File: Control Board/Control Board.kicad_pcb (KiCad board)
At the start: 2 copper layers, 80 x 58.4 mm, 97 parts, among them J1 Conn_02x10_Odd_Even, J10 Conn_01x03, J11 Conn_01x03, J13 Conn_01x03, J14 Conn_01x03, J15 Conn_01x03, J2 Conn_02x03_Odd_Even, J3 RJ45, J4 Conn_01x02, J5 Conn_01x02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

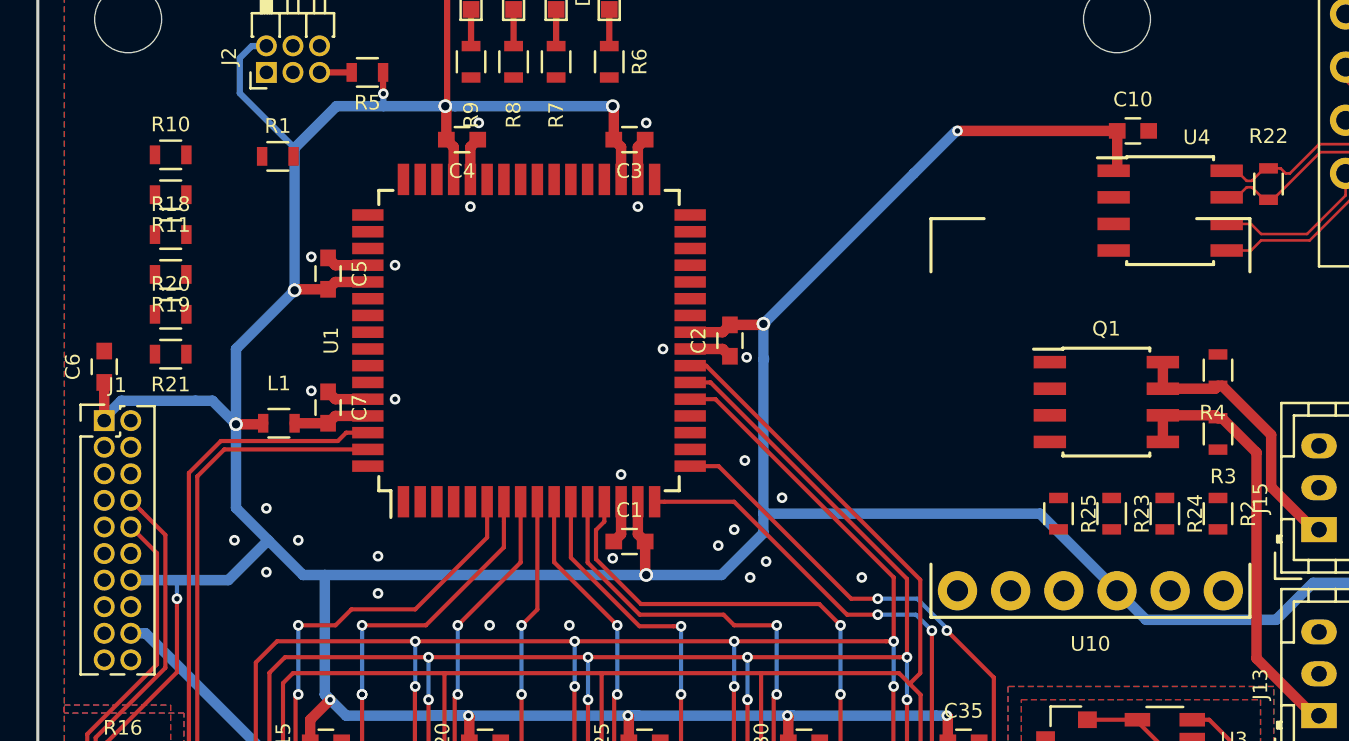
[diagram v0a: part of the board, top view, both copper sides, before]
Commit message: Added comments and stuff for power board PCB review
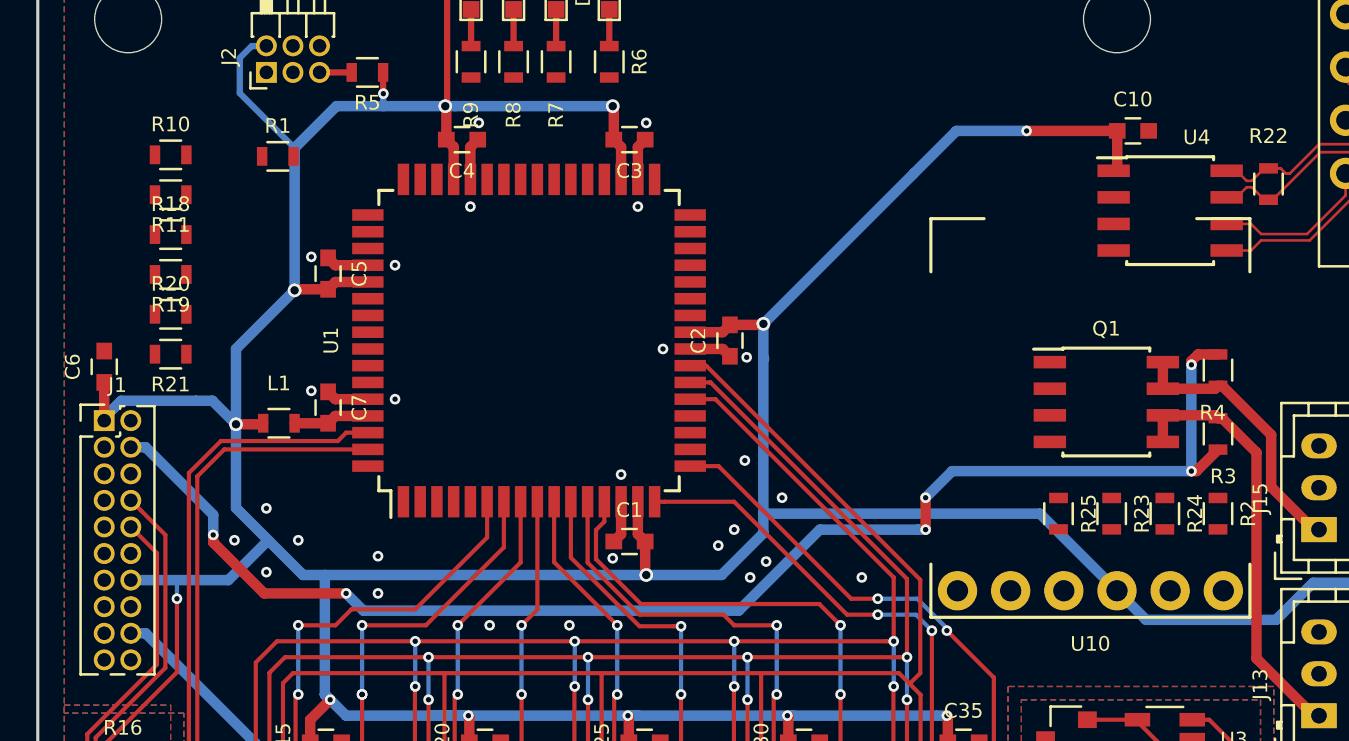
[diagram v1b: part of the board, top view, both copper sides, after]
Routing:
- net /VCC_IN: track 0.00 -> 66.7 mm, vias 0 -> 6
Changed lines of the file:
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@@
     (thickness 1.6)
     (drawings 25)
-    (tracks 765)
+    (tracks 794)
     (zones 0)
     (modules 97)
@@
     (effects (font (size 1 1) (thickness 0.15)) (justify left mirror))
   )
+  (segment (start 223.773996 109.982) (end 220.418 109.982) (width 0.5) (layer B.Cu) (net 1))
+  (segment (start 228.104 109.982) (end 223.773996 109.982) (width 0.5) (layer F.Cu) (net 1))
+  (via (at 223.773996 109.982) (size 0.508) (drill 0.254) (layers F.Cu B.Cu) (net 1))
   (segment (start 245.11 137.922) (end 244.86 137.922) (width 0.5) (layer B.Cu) (net 1))
   (segment (start 244.86 137.922) (end 242.32 135.382) (width 0.5) (layer B.Cu) (net 1))
@@
   (segment (start 244.86 129.032) (end 245.11 129.032) (width 0.5) (layer B.Cu) (net 1))
   (segment (start 218.386 112.014) (end 220.418 109.982) (width 0.5) (layer B.Cu) (net 1))
-  (segment (start 228.104 109.982) (end 220.472 109.982) (width 0.5) (layer F.Cu) (net 1))
-  (via (at 220.472 109.982) (size 0.508) (drill 0.254) (layers F.Cu B.Cu) (net 1))
   (segment (start 228.104 109.982) (end 228.104 111.715) (width 0.5) (layer F.Cu) (net 1))
   (segment (start 228.104 111.715) (end 227.932 111.887) (width 0.5) (layer F.Cu) (net 1))
@@
   (via (at 188.976 133.604) (size 0.508) (drill 0.254) (layers F.Cu B.Cu) (net 68))
   (segment (start 188.976 136.906) (end 188.976 133.604) (width 0.2) (layer B.Cu) (net 68))
+  (segment (start 231.648 120.982) (end 231.648 121.158006) (width 0.5) (layer F.Cu) (net 69))
+  (segment (start 232.918 120.662) (end 231.968 120.662) (width 0.5) (layer F.Cu) (net 69))
+  (segment (start 231.968 120.662) (end 231.648 120.982) (width 0.5) (layer F.Cu) (net 69))
+  (segment (start 231.648 126.238) (end 231.648 121.158006) (width 0.5) (layer B.Cu) (net 69))
+  (via (at 231.648 121.158006) (size 0.508) (drill 0.254) (layers F.Cu B.Cu) (net 69))
+  (segment (start 231.648 126.238) (end 231.89 126.238) (width 0.5) (layer F.Cu) (net 69))
+  (segment (start 231.89 126.238) (end 232.918 125.21) (width 0.5) (layer F.Cu) (net 69))
+  (segment (start 218.948 127.508) (end 220.218 126.238) (width 0.5) (layer B.Cu) (net 69))
+  (segment (start 220.218 126.238) (end 231.648 126.238) (width 0.5) (layer B.Cu) (net 69))
+  (via (at 231.648 126.238) (size 0.508) (drill 0.254) (layers F.Cu B.Cu) (net 69))
+  (segment (start 218.948006 129.032) (end 218.948006 127.508006) (width 0.5) (layer F.Cu) (net 69))
+  (via (at 218.948 127.508) (size 0.508) (drill 0.254) (layers F.Cu B.Cu) (net 69))
+  (segment (start 218.948006 127.508006) (end 218.948 127.508) (width 0.5) (layer F.Cu) (net 69))
+  (via (at 184.912 129.286) (size 0.508) (drill 0.254) (layers F.Cu B.Cu) (net 69))
+  (segment (start 184.912 128.324894) (end 184.912 129.286) (width 0.5) (layer B.Cu) (net 69))
+  (segment (start 181.682106 125.095) (end 184.912 128.324894) (width 0.5) (layer B.Cu) (net 69))
+  (segment (start 180.975 125.095) (end 181.682106 125.095) (width 0.5) (layer B.Cu) (net 69))
+  (via (at 191.262 132.08) (size 0.508) (drill 0.254) (layers F.Cu B.Cu) (net 69))
+  (segment (start 187.34679 132.08) (end 191.262 132.08) (width 0.5) (layer F.Cu) (net 69))
+  (segment (start 184.912 129.64521) (end 187.34679 132.08) (width 0.5) (layer F.Cu) (net 69))
+  (segment (start 184.912 129.286) (end 184.912 129.64521) (width 0.5) (layer F.Cu) (net 69))
+  (via (at 218.948006 129.032) (size 0.508) (drill 0.254) (layers F.Cu B.Cu) (net 69))
+  (segment (start 213.893922 129.032) (end 218.588796 129.032) (width 0.5) (layer B.Cu) (net 69))
+  (segment (start 210.025923 132.899999) (end 213.893922 129.032) (width 0.5) (layer B.Cu) (net 69))
+  (segment (start 218.588796 129.032) (end 218.948006 129.032) (width 0.5) (layer B.Cu) (net 69))
+  (segment (start 191.262 132.08) (end 192.081999 132.899999) (width 0.5) (layer B.Cu) (net 69))
+  (segment (start 192.081999 132.899999) (end 210.025923 132.899999) (width 0.5) (layer B.Cu) (net 69))
+  (segment (start 218.948 129.031994) (end 218.948006 129.032) (width 0.5) (layer F.Cu) (net 69))
   (segment (start 190.4 123.95) (end 188.8 123.95) (width 0.5) (layer F.Cu) (net 70))
   (segment (start 190.4 123.95) (end 190.75 123.6) (width 0.5) (layer F.Cu) (net 70))
